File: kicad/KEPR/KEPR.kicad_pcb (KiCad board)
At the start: 2 copper layers, 329.5 x 199.5 mm, 32 parts, among them J1 PINHD_1x20_Male, J10 Conn_02x40_Odd_Even, J11 10141995-005RLF, J12 PINHD_1x20_Male, J16 PINHD_1x10_Male, J17 PINHD_1x20_Male, J19 PINHD_1x20_Male, J22 Barrel_Jack, J23 PINHD_1x10_Male, J24 PINHD_2x3_Male, J26 PINHD_2x3_Male, J3 Conn_02x12_Odd_Even, J30 PINHD_2x3_Male, J4 Conn_02x15_Odd_Even, J5 Conn_02x08_Odd_Even, J6 Conn_02x20_Odd_Even, J9 Conn_02x40_Odd_Even, U2 STM32G484CETx

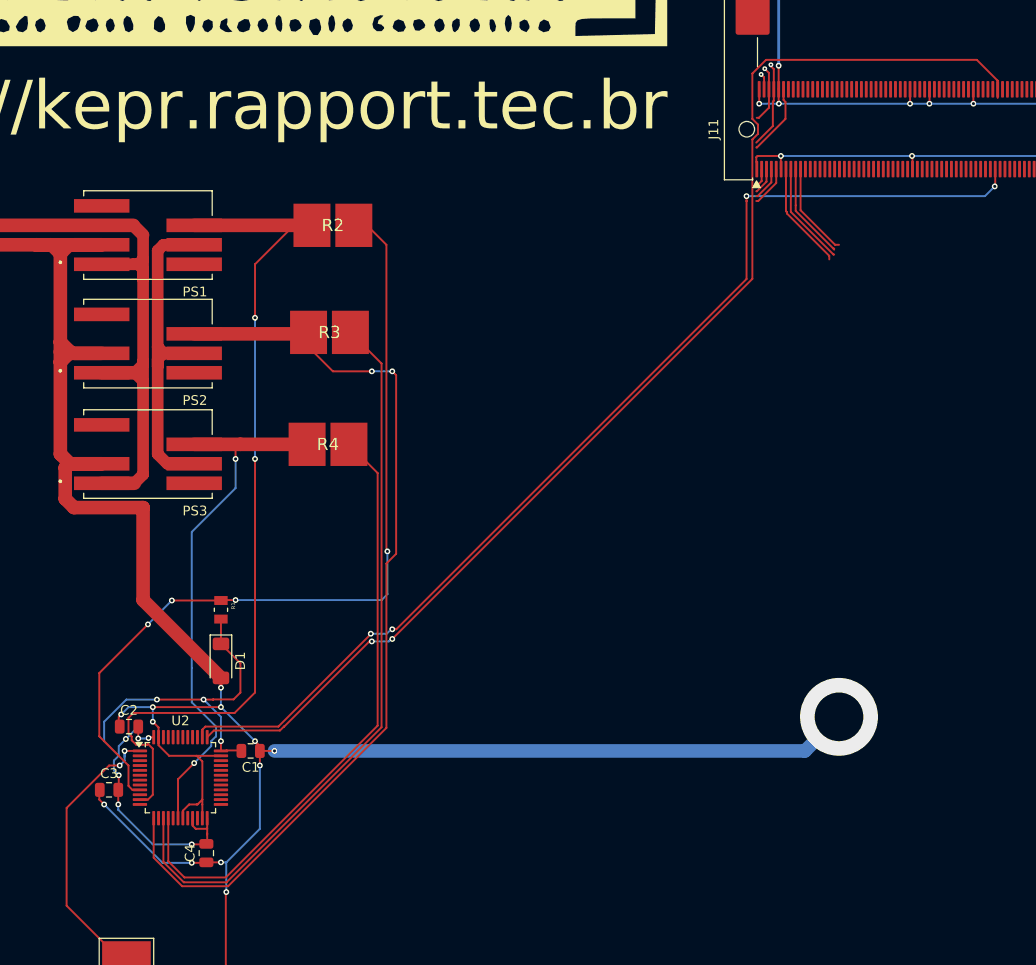
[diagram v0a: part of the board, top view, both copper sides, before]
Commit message: Troca dos sensores de corrente e conversores de tensão para o MCU controlador
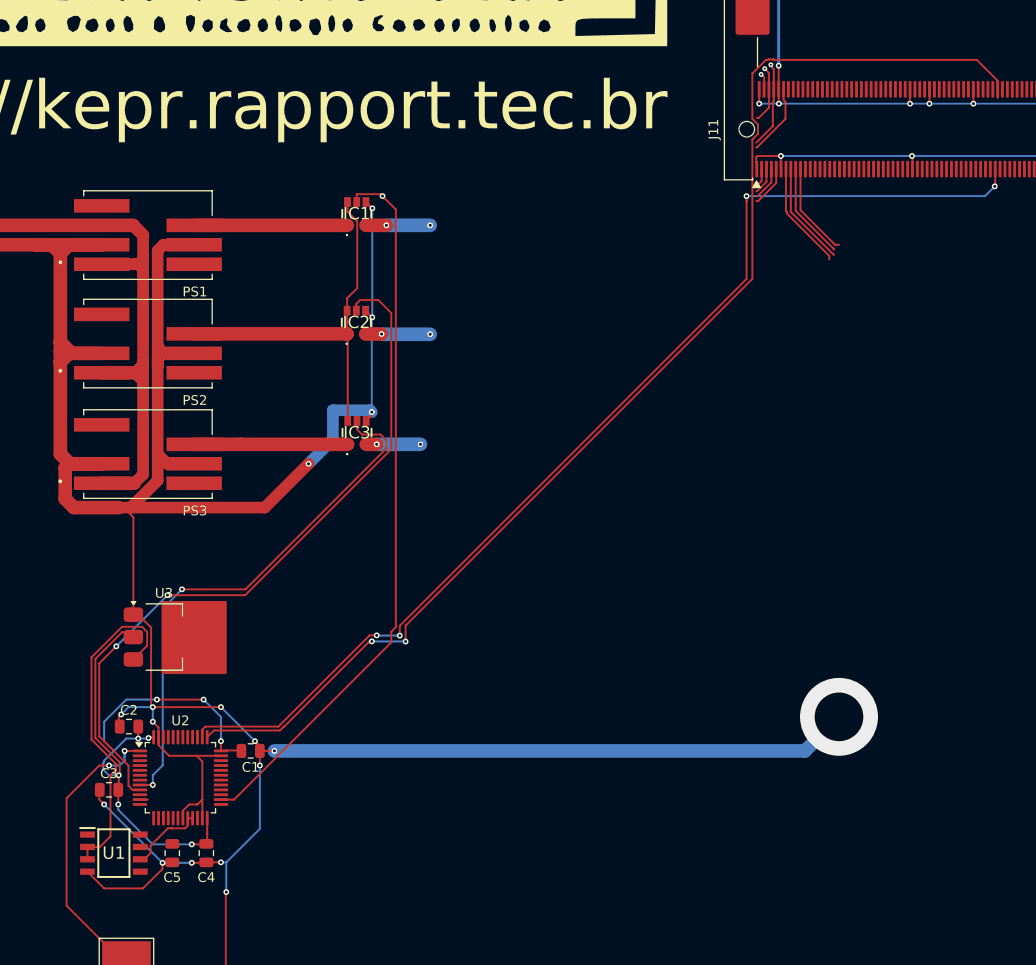
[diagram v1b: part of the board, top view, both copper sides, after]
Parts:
- removed D1: BZV55B3V3, Diode_SMD:D_MiniMELF
- removed R1: 5.6MR, Resistors SMD:RESC2012X60N
- removed R2: GMR320HJAAFM5L00, Shunt Rohm:RESC7142X55N
- removed R3: GMR320HJAAFS5L00, Shunt Rohm:RESC7142X55N
- removed R4: GMR320HJAAFE5L00, Shunt Rohm:RESC7142X55N
- added C5: 1uF_Ceramic, Capacitor:C_0805_2012Metric, F.Cu at (96.5, 140.5)
- added IC1: ACS37041KLHBLT-010B3, ACS37041:APS12628LLHALTBAP, F.Cu at (115.5, 74.8)
- added IC2: ACS37041KLHBLT-010B3, ACS37041:APS12628LLHALTBAP, F.Cu at (115.4, 86.0)
- added IC3: ACS37041KLHBLT-010B3, ACS37041:APS12628LLHALTBAP, F.Cu at (115.5, 97.3)
- added U1: REF193, REF193:SOIC127P600X175-8N, F.Cu at (90.5, 140.5)
- added U3: AMS1117-3.3, Package_TO_SOT_SMD:SOT-223-3_TabPin2, F.Cu at (95.7, 118.3)
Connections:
- C1 pad 2: /UCE board/VDD_Z_MCU_CTL_3v3 -> /UCE board/VDD_MCU_CTL_3v3
- C2 pad 2: /UCE board/VDD_Z_MCU_CTL_3v3 -> /UCE board/VDD_MCU_CTL_3v3
- C3 pad 2: /UCE board/VDD_Z_MCU_CTL_3v3 -> /UCE board/VDD_MCU_CTL_3v3
- C4 pad 2: /UCE board/VDD_Z_MCU_CTL_3v3 -> /UCE board/VDD_MCU_CTL_3v3
- U2 pad 11: +3v3 Shunt -> unconnected-(U2-PA3-Pad11)
- U2 pad 13: +5v Shunt -> unconnected-(U2-PA5-Pad13)
- U2 pad 15: +5V -> unconnected-(U2-PA7-Pad15)
- U2 pad 16: +12V -> unconnected-(U2-PB0-Pad16)
- U2 pad 18: +12v Shunt -> unconnected-(U2-PB2-Pad18)
- U2 pad 20: unconnected-(U2-VREF+-Pad20) -> /UCE board/VDDA_MCU_CTL_3
- U2 pad 21: /UCE board/VDD_Z_MCU_CTL_3v3 -> /UCE board/VDDA_MCU_CTL_3
- U2 pad 24: /UCE board/VDD_Z_MCU_CTL_3v3 -> /UCE board/VDD_MCU_CTL_3v3
- U2 pad 26: unconnected-(U2-PB12-Pad26) -> /UCE board/+3.3v Shunt Out
- U2 pad 36: /UCE board/VDD_Z_MCU_CTL_3v3 -> /UCE board/VDD_MCU_CTL_3v3
- U2 pad 48: /UCE board/VDD_Z_MCU_CTL_3v3 -> /UCE board/VDD_MCU_CTL_3v3
- U2 pad 8: unconnected-(U2-PA0-Pad8) -> /UCE board/+12v Shunt Out
- U2 pad 9: /UCE board/+3.3v Shunt Out -> /UCE board/+5v Shunt Out
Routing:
- net +3.3V: track 87.3 -> 6.60 mm, vias 4 -> 2
- net /UCE board/+3.3v Shunt Out: track 0.00 -> 74.3 mm, vias 0 -> 1
- net /UCE board/+5v Shunt Out: track 0.00 -> 73.5 mm, vias 0 -> 2
- net +5V: track 76.3 -> 6.68 mm, vias 0 -> 2
- net GND: track 2008.0 -> 2077.5 mm, vias 47 -> 51
- net /UCE board/VDD_MCU_CTL_3v3: track 0.00 -> 68.9 mm, vias 0 -> 8
- net +3v3 Shunt: track 91.2 -> 23.4 mm, vias 2 -> 0
- net /UCE board/VDD_Z_MCU_CTL_3v3: track 65.4 -> 0.00 mm, vias 9 -> 0
- net /UCE board/+12v Shunt Out: track 0.00 -> 54.9 mm, vias 0 -> 2
- net +5v Shunt: track 96.1 -> 43.1 mm, vias 2 -> 0
- net +12v Shunt: track 54.7 -> 16.5 mm, vias 2 -> 0
- net +12V: track 63.2 -> 40.1 mm, vias 0 -> 2
- net /UCE board/VDDA_MCU_CTL_3: track 0.00 -> 8.17 mm
- net I2C_SDA_MCU_CTL: track 125.5 -> 126.5 mm
- net unconnected-(U2-PA3-Pad11): track 0.00 -> 0.83 mm
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
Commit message: Atualizado informações para a versão 0.6
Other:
- board text added: "KEPR V0.6 2025"
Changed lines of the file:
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@@
 		(title "UCE Board")
 		(date "2026-01-01")
-		(rev "0.5")
+		(rev "0.6")
 		(company "Rapport Tecnologia")
 		(comment 1 "Carlos Delfino Carvalho Pinheiro")
@@
 		)
 	)
+	(gr_text "KEPR V0.6\n2025"
+		(at 42.5 93.5 0)
+		(layer "F.SilkS")
+		(effects
+			(font
+				(size 7 5)
+				(thickness 1.25)
+				(bold yes)
+			)
+			(justify left bottom)
+		)
+	)

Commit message: Iniciado a distribuição das vias.
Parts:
- added U4: AMS1117-1.8, Package_TO_SOT_SMD:SOT-223-3_TabPin2, F.Cu at (127.0, 70.0)
- C5: value 1uF_Ceramic -> 0.1nF_Ceramic
- J3: footprint Connector_IDC:IDC-Header_2x25_P2.54mm_Latch6.5mm_Vertical -> Connector_IDC:IDC-Header_2x12_P2.54mm_Latch9.5mm_Vertical
- moved J16 25.2 mm to (318.5, 215.0)
- moved J30 25.0 mm to (327.4, 209.0)
- moved J23 25.0 mm to (318.5, 218.9)
- moved J6 3.13 mm to (342.9, 196.0)
- moved J9 2.66 mm to (56.6, 198.5)
- moved J10 2.59 mm to (175.0, 198.5)
- moved J12 1.84 mm to (175.3, 214.9)
- moved J19 1.84 mm to (175.3, 218.9)
- moved J26 0.38 mm to (195.8, 208.6)
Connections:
- net /Power/External Power Rails/UCE_MCU_VCTL_12v renamed /Power/Power Rails/UCE_MCU_VCTL_12v
- net /Power/External Power Rails/UCE_MCU_VCTL_3v3 renamed /Power/Power Rails/UCE_MCU_VCTL_3v3
- net /Power/External Power Rails/UCE_MCU_VCTL_5V renamed /Power/Power Rails/UCE_MCU_VCTL_5V
- net /Power/External Power Rails/Vout_external_1 renamed /Power/Power Rails/Vout_external_1
- net /Power/External Power Rails/Vout_external_2 renamed /Power/Power Rails/Vout_external_2
- net /Power/External Power Rails/Vout_external_3 renamed /Power/Power Rails/Vout_external_3
- J10 pad 11: GND -> +12V
- J10 pad 12: GND -> +12V
- J10 pad 13: VCC_5V -> +5V
- J10 pad 14: VCC_5V -> +5V
- J10 pad 51: VCC_5V -> +5V
- J10 pad 52: VCC_5V -> +5V
- J10 pad 65: RESERVED -> unconnected-(J10-Pin_65-Pad65)
- J10 pad 67: RESERVED -> unconnected-(J10-Pin_67-Pad67)
- J10 pad 68: RESERVED -> unconnected-(J10-Pin_68-Pad68)
- J10 pad 69: RESERVED -> unconnected-(J10-Pin_69-Pad69)
- J10 pad 7: RESERVED -> GND
- J10 pad 70: RESERVED -> unconnected-(J10-Pin_70-Pad70)
- J10 pad 71: RESERVED -> unconnected-(J10-Pin_71-Pad71)
- J10 pad 72: RESERVED -> unconnected-(J10-Pin_72-Pad72)
- J10 pad 73: RESERVED -> unconnected-(J10-Pin_73-Pad73)
- J10 pad 74: RESERVED -> unconnected-(J10-Pin_74-Pad74)
- J10 pad 75: RESERVED -> unconnected-(J10-Pin_75-Pad75)
- J10 pad 76: RESERVED -> unconnected-(J10-Pin_76-Pad76)
- J10 pad 8: RESERVED -> GND
- J11 pad 134: VCC_5V -> +5V
- J11 pad 197: VCC_5V -> +5V
- J11 pad 223: VCC_5V -> +5V
- J11 pad 3: VCC_5V -> +5V
- J11 pad 53: NET_CMD_EVEN -> NET_D2_EVEN
- J11 pad 66: VCC_5V -> +5V
- J11 pad 92: VCC_5V -> +5V
- J3 pad 12: NET_CMD_EVEN -> NET_D1_EVEN
- J3 pad 14: NET_CMD_EVEN -> NET_D2_EVEN
- J3 pad 16: NET_CMD_EVEN -> NET_D2_EVEN
- J3 pad 22: NET_CMD_EVEN -> NET_CTL2_EVEN
- J4 pad 23: NET_CMD_EVEN -> unconnected-(J4-Pin_23-Pad23)
- J4 pad 24: NET_CMD_EVEN -> unconnected-(J4-Pin_24-Pad24)
- J4 pad 25: NET_CMD_EVEN -> unconnected-(J4-Pin_25-Pad25)
- J4 pad 26: NET_CMD_EVEN -> unconnected-(J4-Pin_26-Pad26)
- J4 pad 27: NET_CMD_EVEN -> unconnected-(J4-Pin_27-Pad27)
- J4 pad 28: NET_CMD_EVEN -> unconnected-(J4-Pin_28-Pad28)
- J5 pad 13: NET_CMD_EVEN -> unconnected-(J5-Pin_13-Pad13)
- J5 pad 15: NET_CMD_EVEN -> unconnected-(J5-Pin_15-Pad15)
- J6 pad 10: VCC_3V3 -> VCC_1V8
- J6 pad 5: VCC_5V -> +5V
- J6 pad 6: VCC_5V -> +5V
- J6 pad 8: VCC_1V8 -> VCC_3V3
- J9 pad 1: GND -> unconnected-(J9-Pin_1-Pad1)
- J9 pad 10: VCC_3V3 -> VCC_1V8
- J9 pad 11: VREF_IO -> VCC_1V8
- J9 pad 12: VREF_IO -> VCC_3V3
- J9 pad 13: UART3_TX -> VREF_IO
- J9 pad 14: UART3_RX -> VREF_IO
- J9 pad 15: UART0_CTS -> UART3_TX
- J9 pad 16: UART0_RTS -> UART3_RX
- J9 pad 17: UART0_DSR -> UART0_CTS
- J9 pad 18: UART0_DCD -> UART0_RTS
- J9 pad 19: UART0_RI -> UART0_DSR
- J9 pad 2: GND -> unconnected-(J9-Pin_2-Pad2)
- J9 pad 20: GND -> UART0_DCD
- J9 pad 21: SPI0_SCK -> UART0_RI
- J9 pad 22: SPI0_MOSI -> GND
- J9 pad 23: SPI0_MISO -> SPI0_SCK
- J9 pad 24: SPI0_CS0 -> SPI0_MOSI
- J9 pad 25: SPI0_CS1 -> SPI0_MISO
- J9 pad 26: SPI0_CS2 -> SPI0_CS0
- J9 pad 27: SPI1_SCK -> SPI0_CS1
- J9 pad 28: SPI1_MOSI -> SPI0_CS2
- J9 pad 29: SPI1_MISO -> SPI1_SCK
- J9 pad 30: SPI1_CS0 -> SPI1_MOSI
- J9 pad 31: SPI1_CS1 -> SPI1_MISO
- J9 pad 32: SPI1_CS2 -> SPI1_CS0
- J9 pad 33: GPIO0 -> SPI1_CS1
- J9 pad 34: GPIO8 -> SPI1_CS2
- J9 pad 35: GPIO1 -> GPIO0
- J9 pad 36: GPIO9 -> GPIO8
- J9 pad 37: GPIO2 -> GPIO1
- J9 pad 38: GPIO10 -> GPIO9
- J9 pad 39: GPIO3 -> GPIO2
- J9 pad 40: GPIO11 -> GPIO10
- J9 pad 41: GPIO4 -> GPIO3
- J9 pad 42: GPIO12 -> GPIO11
- J9 pad 43: GPIO5 -> GPIO4
- J9 pad 44: GPIO13 -> GPIO12
- J9 pad 45: GPIO6 -> GPIO5
- J9 pad 46: GPIO14 -> GPIO13
- J9 pad 47: GPIO7 -> GPIO6
- J9 pad 48: GPIO15 -> GPIO14
- J9 pad 49: PWM0 -> GPIO7
- J9 pad 5: VCC_5V -> GND
- J9 pad 50: PWM4 -> GPIO15
- J9 pad 51: PWM1 -> PWM0
- J9 pad 52: PWM5 -> PWM4
- J9 pad 53: PWM2 -> PWM1
- J9 pad 54: PWM6 -> PWM5
- J9 pad 55: PWM3 -> PWM2
- J9 pad 56: PWM7 -> PWM6
- J9 pad 57: IR_RX_IN -> PWM3
- J9 pad 58: IR_TX_OUT -> PWM7
- J9 pad 59: AIN0 -> IR_RX_IN
- J9 pad 6: VCC_5V -> GND
- J9 pad 60: AIN4 -> IR_TX_OUT
- J9 pad 61: AIN1 -> AIN0
- J9 pad 62: AIN5 -> AIN4
- J9 pad 63: AIN2 -> AIN1
- J9 pad 64: AIN6 -> AIN5
- J9 pad 65: AIN3 -> AIN2
- J9 pad 66: AIN7 -> AIN6
- J9 pad 67: AOUT0 -> AIN3
- J9 pad 68: AOUT1 -> AIN7
- J9 pad 69: I2S_BCLK -> AOUT0
- J9 pad 7: VCC_3V3 -> +5V
- J9 pad 70: I2S_LRCLK -> AOUT1
- J9 pad 71: I2S_DOUT -> I2S_BCLK
- J9 pad 72: I2S_DIN -> I2S_LRCLK
- J9 pad 73: I2S_MCLK -> I2S_DOUT
- J9 pad 74: GND -> I2S_DIN
- J9 pad 75: RESERVED -> I2S_MCLK
- J9 pad 76: RESERVED -> GND
- J9 pad 8: VCC_1V8 -> +5V
- J9 pad 9: VCC_1V8 -> VCC_3V3
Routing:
- net I2C2_SCL: track 9.95 -> 231.2 mm, vias 0 -> 2
- net +5V: track 6.68 -> 224.2 mm, vias 2 -> 3
- net +3.3V: track 6.60 -> 196.0 mm, vias 2 -> 5
- net MCU_BOOT0: track 0.00 -> 188.5 mm
- net I2C0_SCL: track 10.7 -> 192.2 mm, vias 0 -> 2
- net GND: track 2077.5 -> 2233.5 mm, vias 51 -> 59
- net +12V: track 40.1 -> 190.2 mm
- net DBG_TCK: track 0.00 -> 107.9 mm, vias 0 -> 4
- net DBG_TDO: track 0.00 -> 72.5 mm, vias 0 -> 2
- net DBG_TMS: track 0.00 -> 71.1 mm, vias 0 -> 2
- net DBG_VREF: track 0.00 -> 68.3 mm
- net VCC_IN: track 7.34 -> 69.6 mm, vias 0 -> 1
- net +24V: track 109.8 -> 164.7 mm
- net I2C1_SCL: track 0.00 -> 50.7 mm, vias 0 -> 1
- net MCU_RST_N: track 11.1 -> 60.3 mm, vias 0 -> 4
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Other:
- board size 329.5 x 199.5 mm -> 347.5 x 199.5 mm

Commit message: Ajustes para o MCU Board STM32N6
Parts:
- added J13: 10141995-005RLF, SODIMM DDR4 EDGE 260 pins:SODIMM_DDR4_EDGE, F.Cu at (176.0, 133.0)
- J24, J30: value PINHD_2x3_Male -> PINHD_2x2_Male; footprint Connector_PinHeader_2.54mm:PinHeader_2x03_P2.54mm_Vertical -> Connector_PinHeader_2.54mm:PinHeader_2x02_P2.54mm_Vertical
- moved C1 112.9 mm to (126.5, 240.8)
- moved C2 112.9 mm to (114.0, 238.3)
- moved C3 112.9 mm to (112.0, 244.8)
- moved C4 112.9 mm to (122.0, 251.3)
- moved C5 112.9 mm to (118.5, 251.3)
- moved G*** 112.9 mm to (122.0, 152.3)
- moved IC2 112.9 mm to (137.4, 196.7)
- moved J10 112.9 mm to (197.0, 309.3)
- moved J12 112.9 mm to (197.3, 325.7)
- moved J17 112.9 mm to (76.0, 329.7)
- moved J19 112.9 mm to (197.3, 329.7)
- moved J22 112.9 mm to (69.5, 161.3)
- moved J23 112.9 mm to (340.5, 329.7)
- moved J24 112.9 mm to (97.7, 319.8)
- moved J26 112.9 mm to (217.8, 319.4)
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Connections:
- J24 pad 1: /Power/Power Rails/Vout_external_1 -> unconnected-(J24-Pad1)
- J24 pad 2: +12V -> unconnected-(J24-Pad2)
- J24 pad 3: /Power/Power Rails/Vout_external_1 -> unconnected-(J24-Pad3)
- J24 pad 4: +5V -> unconnected-(J24-Pad4)
- J30 pad 1: /Power/Power Rails/Vout_external_3 -> unconnected-(J30-Pad1)
- J30 pad 2: +12V -> unconnected-(J30-Pad2)
- J30 pad 3: /Power/Power Rails/Vout_external_3 -> unconnected-(J30-Pad3)
- J30 pad 4: +5V -> unconnected-(J30-Pad4)
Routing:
- net MCU_BOOT0: track 188.5 -> 187.1 mm
- net I2C2_SCL: track 231.2 -> 232.5 mm
- net I2C_SCL_MCU_CTL: track 112.7 -> 111.7 mm
- net I2C0_SCL: track 192.2 -> 193.2 mm
- net UART1_TX: track 42.1 -> 42.9 mm
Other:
- board size 347.5 x 199.5 mm -> 329.5 x 230.1 mm

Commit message: ainda fazendo testes de composição das placas.
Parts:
- removed J13: 10141995-005RLF, SODIMM DDR4 EDGE 260 pins:SODIMM_DDR4_EDGE
- moved BT1 108.4 mm to (62.0, 180.5), turned to 90 degrees
- moved C1 106.9 mm to (121.0, 134.0)
- moved C2 106.9 mm to (108.5, 131.5)
- moved C3 106.9 mm to (106.5, 138.0)
- moved C4 106.9 mm to (116.5, 144.5)
- moved C5 106.9 mm to (113.0, 144.5)
- moved G*** 106.9 mm to (116.5, 45.5)
- moved IC2 106.9 mm to (131.9, 90.0)
- moved J10 106.9 mm to (191.5, 202.5)
- moved J12 106.9 mm to (191.8, 218.9)
- moved J17 106.9 mm to (70.5, 222.9)
- moved J19 106.9 mm to (191.8, 222.9)
- moved J22 106.9 mm to (64.0, 54.5)
- moved J23 106.9 mm to (335.0, 222.9)
- moved J24 106.9 mm to (92.2, 213.0)
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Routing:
- net GND: track 2233.5 -> 2278.0 mm
- net Net-(BT1-+): track 60.3 -> 97.1 mm
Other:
- board size 329.5 x 230.1 mm -> 329.5 x 199.5 mm

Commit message: Diversos ajustes no barramento e ampliação das trilhas na PCB
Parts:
- added J13: PINHD_2x2_Male, Connector_PinHeader_2.54mm:PinHeader_2x02_P2.54mm_Vertical, F.Cu at (258.0, 186.5)
- moved J11 12.9 mm to (204.4, 75.0)
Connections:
- J10 pad 15: VCC_3V3 -> +3.3V
- J10 pad 16: VCC_3V3 -> +3.3V
- J10 pad 17: VCC_1V8 -> +1v8
- J10 pad 18: VCC_1V8 -> +1v8
- J10 pad 53: VCC_3V3 -> +3.3V
- J10 pad 54: VCC_1V8 -> +3.3V
- J10 pad 55: VCC_1V8 -> +1v8
- J10 pad 56: VCC_3V3 -> +1v8
- J11 pad 135: VCC_1V8 -> +1v8
- J11 pad 136: VCC_3V3 -> +3.3V
- J11 pad 198: VCC_3V3 -> +3.3V
- J11 pad 199: VCC_1V8 -> +1v8
- J11 pad 206: RESERVED -> unconnected-(J11-Pad206)
- J11 pad 207: RESERVED -> unconnected-(J11-Pad207)
- J11 pad 208: RESERVED -> unconnected-(J11-Pad208)
- J11 pad 209: RESERVED -> unconnected-(J11-Pad209)
- J11 pad 210: RESERVED -> unconnected-(J11-Pad210)
- J11 pad 211: RESERVED -> unconnected-(J11-Pad211)
- J11 pad 212: RESERVED -> unconnected-(J11-Pad212)
- J11 pad 213: RESERVED -> unconnected-(J11-Pad213)
- J11 pad 224: VCC_1V8 -> +1v8
- J11 pad 225: VCC_3V3 -> +3.3V
- J11 pad 4: VCC_3V3 -> +3.3V
- J11 pad 5: VCC_1V8 -> +1v8
- J11 pad 67: VCC_3V3 -> +3.3V
- J11 pad 68: VCC_1V8 -> +1v8
- J11 pad 75: RESERVED -> unconnected-(J11-Pad75)
- J11 pad 76: RESERVED -> unconnected-(J11-Pad76)
- J11 pad 77: RESERVED -> unconnected-(J11-Pad77)
- J11 pad 78: RESERVED -> unconnected-(J11-Pad78)
- J11 pad 79: RESERVED -> unconnected-(J11-Pad79)
- J11 pad 80: RESERVED -> unconnected-(J11-Pad80)
- J11 pad 81: RESERVED -> unconnected-(J11-Pad81)
- J11 pad 82: RESERVED -> unconnected-(J11-Pad82)
- J11 pad 93: VCC_3V3 -> +3.3V
- J11 pad 94: VCC_1V8 -> +1v8
- J3 pad 3: VCC_3V3 -> +3.3V
- J3 pad 4: VCC_3V3 -> +3.3V
- J5 pad 2: VCC_3V3 -> +3.3V
- J6 pad 10: VCC_1V8 -> +1v8
- J6 pad 13: VIO_BANK0 -> unconnected-(J6-Pin_13-Pad13)
- J6 pad 14: VIO_BANK1 -> unconnected-(J6-Pin_14-Pad14)
- J6 pad 15: VIO_BANK2 -> unconnected-(J6-Pin_15-Pad15)
- J6 pad 16: VIO_BANK3 -> unconnected-(J6-Pin_16-Pad16)
- J6 pad 17: PWR_GOOD -> unconnected-(J6-Pin_17-Pad17)
- J6 pad 7: VCC_3V3 -> +3.3V
- J6 pad 8: VCC_3V3 -> +3.3V
- J6 pad 9: VCC_1V8 -> +1v8
- J9 pad 1: unconnected-(J9-Pin_1-Pad1) -> GND
- J9 pad 10: VCC_1V8 -> +3.3V
- J9 pad 11: VCC_1V8 -> +1v8
- J9 pad 12: VCC_3V3 -> +1v8
- J9 pad 2: unconnected-(J9-Pin_2-Pad2) -> GND
- J9 pad 5: GND -> unconnected-(J9-Pin_5-Pad5)
- J9 pad 51: PWM0 -> unconnected-(J9-Pin_51-Pad51)
- J9 pad 52: PWM4 -> unconnected-(J9-Pin_52-Pad52)
- J9 pad 53: PWM1 -> unconnected-(J9-Pin_53-Pad53)
- J9 pad 54: PWM5 -> unconnected-(J9-Pin_54-Pad54)
- J9 pad 55: PWM2 -> unconnected-(J9-Pin_55-Pad55)
- J9 pad 56: PWM6 -> unconnected-(J9-Pin_56-Pad56)
- J9 pad 57: PWM3 -> unconnected-(J9-Pin_57-Pad57)
- J9 pad 58: PWM7 -> unconnected-(J9-Pin_58-Pad58)
- J9 pad 6: GND -> unconnected-(J9-Pin_6-Pad6)
- J9 pad 9: VCC_3V3 -> +3.3V
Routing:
- net +3.3V: track 196.0 -> 578.2 mm, vias 5 -> 11
- net DBG_SWDIO: track 4.78 -> 251.1 mm, vias 0 -> 1
- net MCU_BOOT0: track 187.1 -> 24.3 mm, vias 0 -> 2
- net VCC_IN: track 69.6 -> 226.2 mm, vias 1 -> 4
- net +5V: track 224.2 -> 355.5 mm, vias 3 -> 6
- net I2C0_SCL: track 193.2 -> 72.9 mm
- net DBG_RESET_N: track 3.52 -> 122.2 mm
- net +1v8: track 0.00 -> 118.2 mm, vias 0 -> 2
- net DBG_TDI: track 4.71 -> 122.6 mm, vias 0 -> 2
- net MOD_TYPE1: track 7.52 -> 122.8 mm, vias 0 -> 1
- net DBG_UART_TX: track 5.55 -> 118.5 mm, vias 0 -> 1
- net DBG_SWCLK: track 7.20 -> 95.2 mm, vias 0 -> 2
- net DBG_UART_RX: track 8.16 -> 95.6 mm, vias 0 -> 2
- net UART3_RX: track 0.00 -> 82.4 mm, vias 0 -> 1
- net PWR_GOOD: track 13.6 -> 82.3 mm
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
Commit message: Adicionado o display oled e mais trilhas.
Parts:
- added Brd1: SSD1306, SSD1306:128x64OLED, F.Cu at (137.7, 137.7)
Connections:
- net /UCE board/VDD_MCU_CTL_3v3 renamed VDD_MCU_CTL_3v3
- net I2C_SCL_MCU_CTL renamed MCU_CTL_I2C_SCL
- net I2C_SDA_MCU_CTL renamed MCU_CTL_I2C_SDA
- J11 pad 138: VIO_BANK1 -> unconnected-(J11-Pad138)
- J11 pad 139: VIO_BANK3 -> unconnected-(J11-Pad139)
- J11 pad 227: VIO_BANK1 -> unconnected-(J11-Pad227)
- J11 pad 228: VIO_BANK3 -> unconnected-(J11-Pad228)
- J11 pad 7: VIO_BANK0 -> unconnected-(J11-Pad7)
- J11 pad 70: VIO_BANK0 -> unconnected-(J11-Pad70)
- J11 pad 71: VIO_BANK2 -> unconnected-(J11-Pad71)
- J11 pad 8: VIO_BANK2 -> unconnected-(J11-Pad8)
- J11 pad 96: VIO_BANK0 -> unconnected-(J11-Pad96)
- J11 pad 97: VIO_BANK2 -> unconnected-(J11-Pad97)
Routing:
- net SDIO_D1: track 0.00 -> 211.3 mm, vias 0 -> 3
- net MCU_BOOT0: track 24.3 -> 205.4 mm, vias 2 -> 3
- net UART3_RX: track 82.4 -> 250.6 mm, vias 1 -> 3
- net MOD_TYPE2: track 60.2 -> 226.0 mm, vias 0 -> 3
- net I2C0_SDA: track 43.8 -> 176.7 mm, vias 0 -> 2
- net UART1_RX: track 36.8 -> 169.3 mm, vias 0 -> 3
- net I2C2_SDA: track 41.4 -> 171.5 mm, vias 0 -> 3
- net UART0_TX: track 32.5 -> 162.6 mm, vias 0 -> 4
- net SDIO_CLK: track 0.00 -> 122.7 mm
- net SDIO_D3: track 0.00 -> 116.9 mm, vias 0 -> 1
- net SDIO_D2: track 0.00 -> 116.6 mm
- net PWR_GOOD: track 82.3 -> 194.5 mm, vias 1 -> 6
- net SDIO_CMD: track 0.00 -> 82.7 mm, vias 0 -> 2
- net +3.3V: track 578.2 -> 652.9 mm, vias 11 -> 13
- net MOD_PRESENT_N: track 56.6 -> 127.8 mm
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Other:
- copper layers 2 -> 4
